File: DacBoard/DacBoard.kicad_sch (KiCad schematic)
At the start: 13 parts, among them J1 DacConnector, U1 74HC00, U2 AD688, U3 74HC00

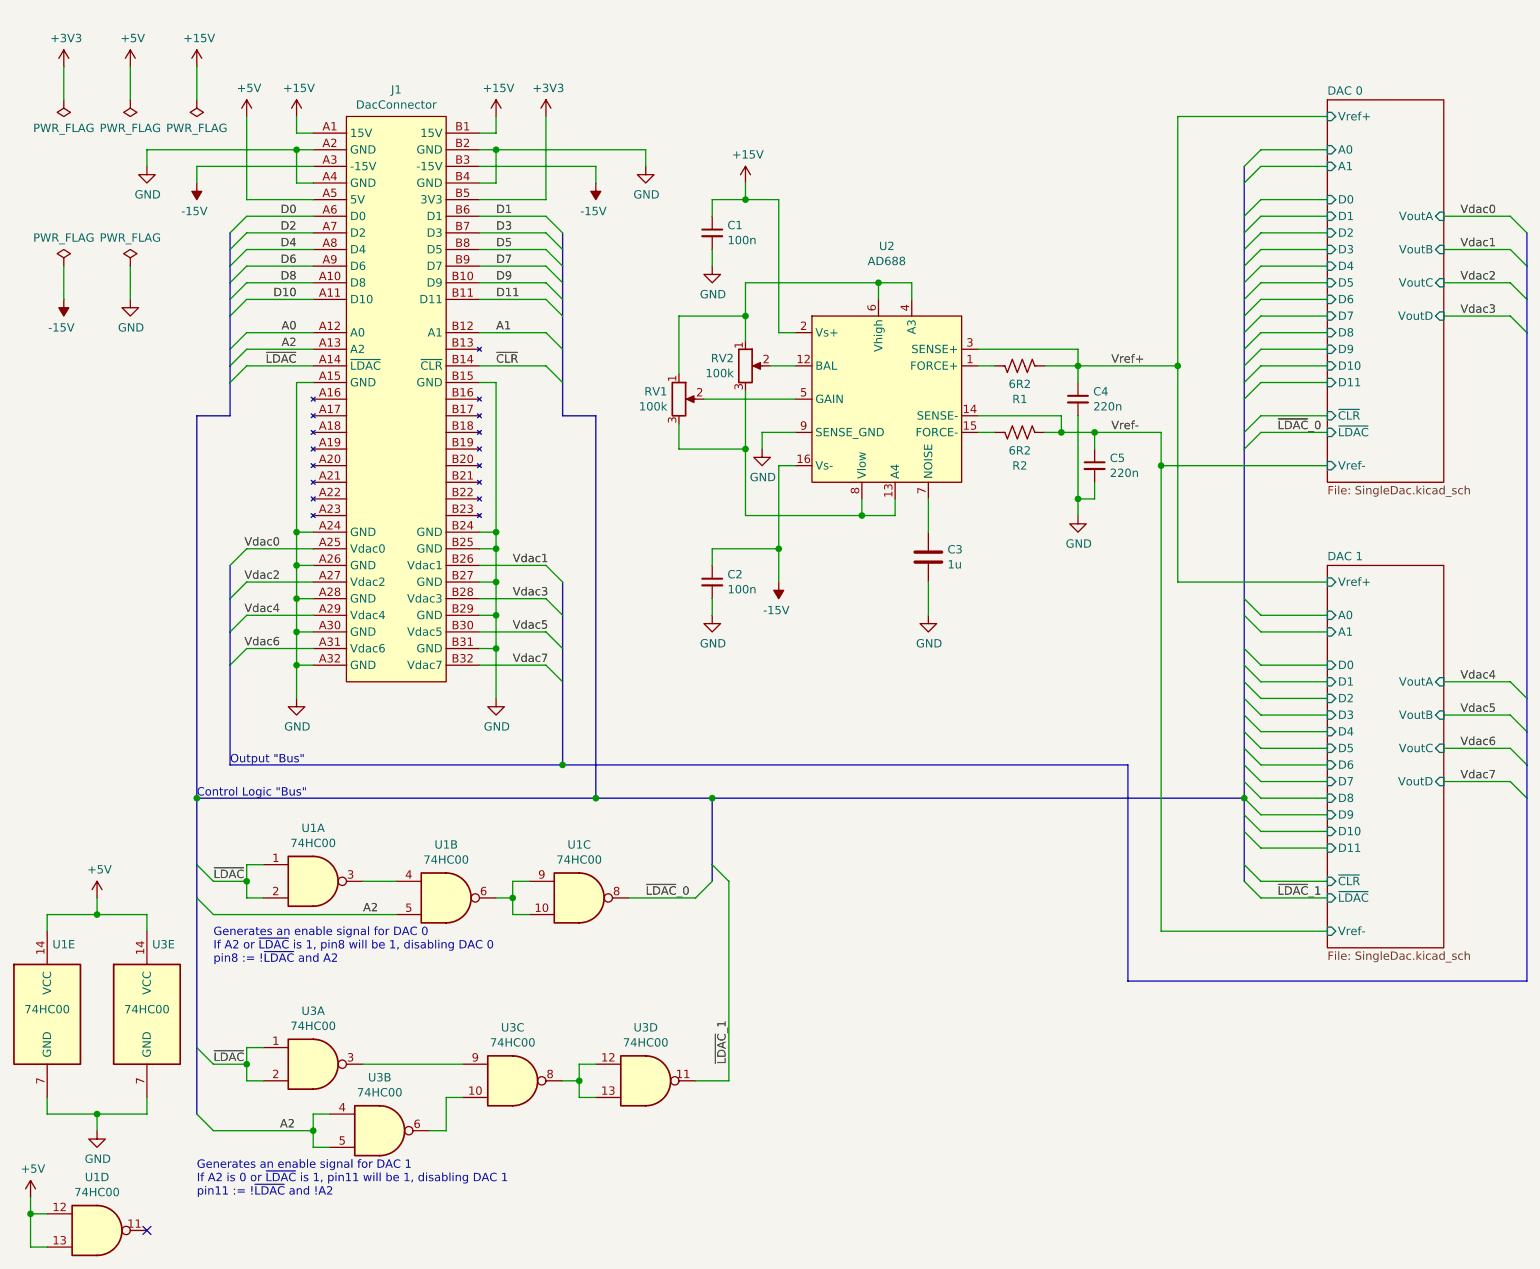
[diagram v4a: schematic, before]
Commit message: Added bypass caps and moved PWR_FLAGs around
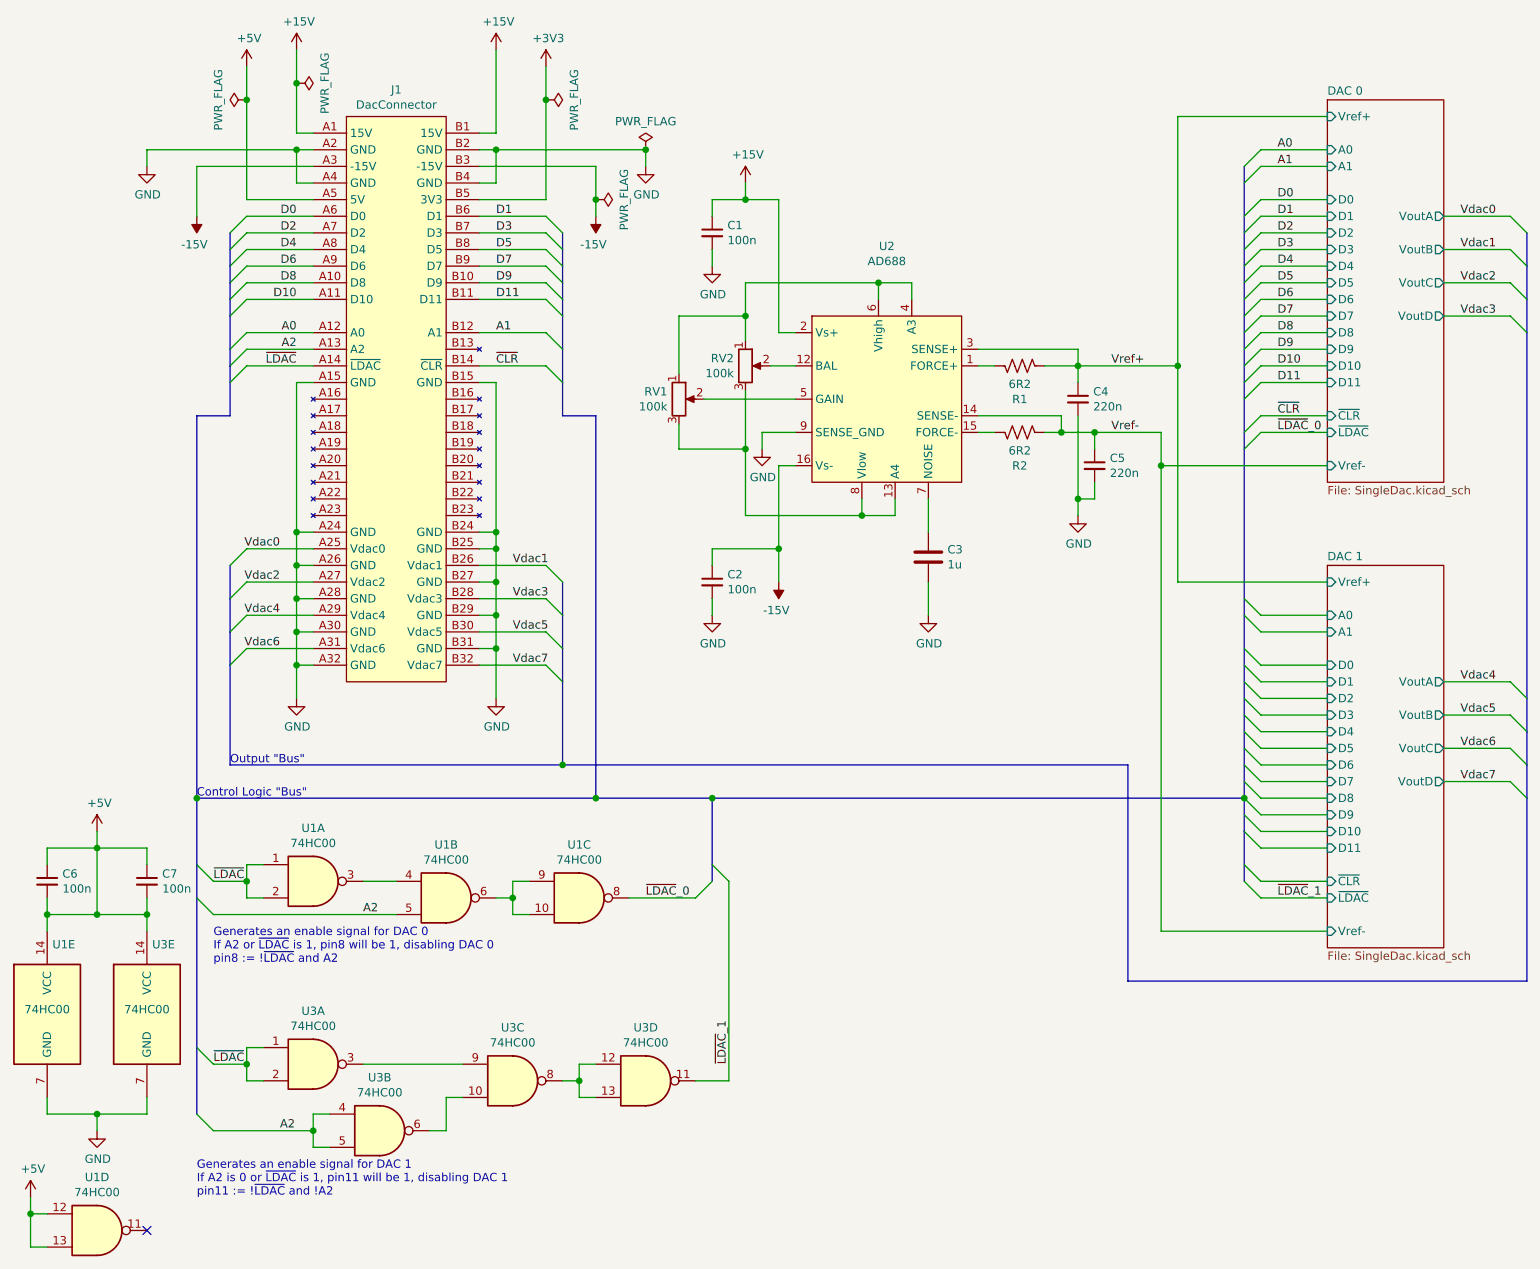
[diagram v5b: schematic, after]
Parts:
- added C6, C7: 100n, symbol Device:C_Small
- C1, C2, C3, C4, C5: footprint (none) -> Capacitor_SMD:C_0805_2012Metric_Pad1.18x1.45mm_HandSolder
- R1, R2: footprint (none) -> Resistor_SMD:R_0805_2012Metric_Pad1.20x1.40mm_HandSolder
- RV1, RV2: footprint (none) -> Potentiometer_SMD:Potentiometer_Bourns_TC33X_Vertical
- U1, U3: footprint (none) -> Package_SO:SOIC-14_3.9x8.7mm_P1.27mm
- U2: footprint (none) -> Package_SO:SOIC-16W_7.5x10.3mm_P1.27mm
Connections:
- net +5V: now also C6.1, C6.2, C7.1, C7.2

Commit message: Fixed description of enable signal generators
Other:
- note added: "Generates an enable signal for DAC 0 If A2 or ~LDAC is 1, pin8 will be 1, disabling DAC 0 pin8 := !(!~LDAC and A2)"
- note added: "Generates an enable signal for DAC 1 If A2 is 0 or ~LDAC is 1, pin11 will be 1, disabling DAC 1 pin11 := !(!~LDAC and !A2)"
- note removed: "Generates an enable signal for DAC 0 If A2 or ~LDAC is 1, pin8 will be 1, disabling DAC 0 pin8 := !~LDAC and A2"
- note removed: "Generates an enable signal for DAC 1 If A2 is 0 or ~LDAC is 1, pin11 will be 1, disabling DAC 1 pin11 := !~LDAC and !A2"
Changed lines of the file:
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@@
     (effects (font (size 1.27 1.27)) (justify left bottom))
   )
-  (text "Generates an enable signal for DAC 1\nIf A2 is 0 or ~LDAC is 1, pin11 will be 1, disabling DAC 1\npin11 := !~LDAC and !A2"
+  (text "Generates an enable signal for DAC 1\nIf A2 is 0 or ~LDAC is 1, pin11 will be 1, disabling DAC 1\npin11 := !(!~LDAC and !A2)"
     (at 40.64 193.04 0)
     (effects (font (size 1.27 1.27)) (justify left bottom))
   )
-  (text "Generates an enable signal for DAC 0\nIf A2 or ~LDAC is 1, pin8 will be 1, disabling DAC 0\npin8 := !~LDAC and A2"
+  (text "Generates an enable signal for DAC 0\nIf A2 or ~LDAC is 1, pin8 will be 1, disabling DAC 0\npin8 := !(!~LDAC and A2)"
     (at 43.18 157.48 0)
     (effects (font (size 1.27 1.27)) (justify left bottom))

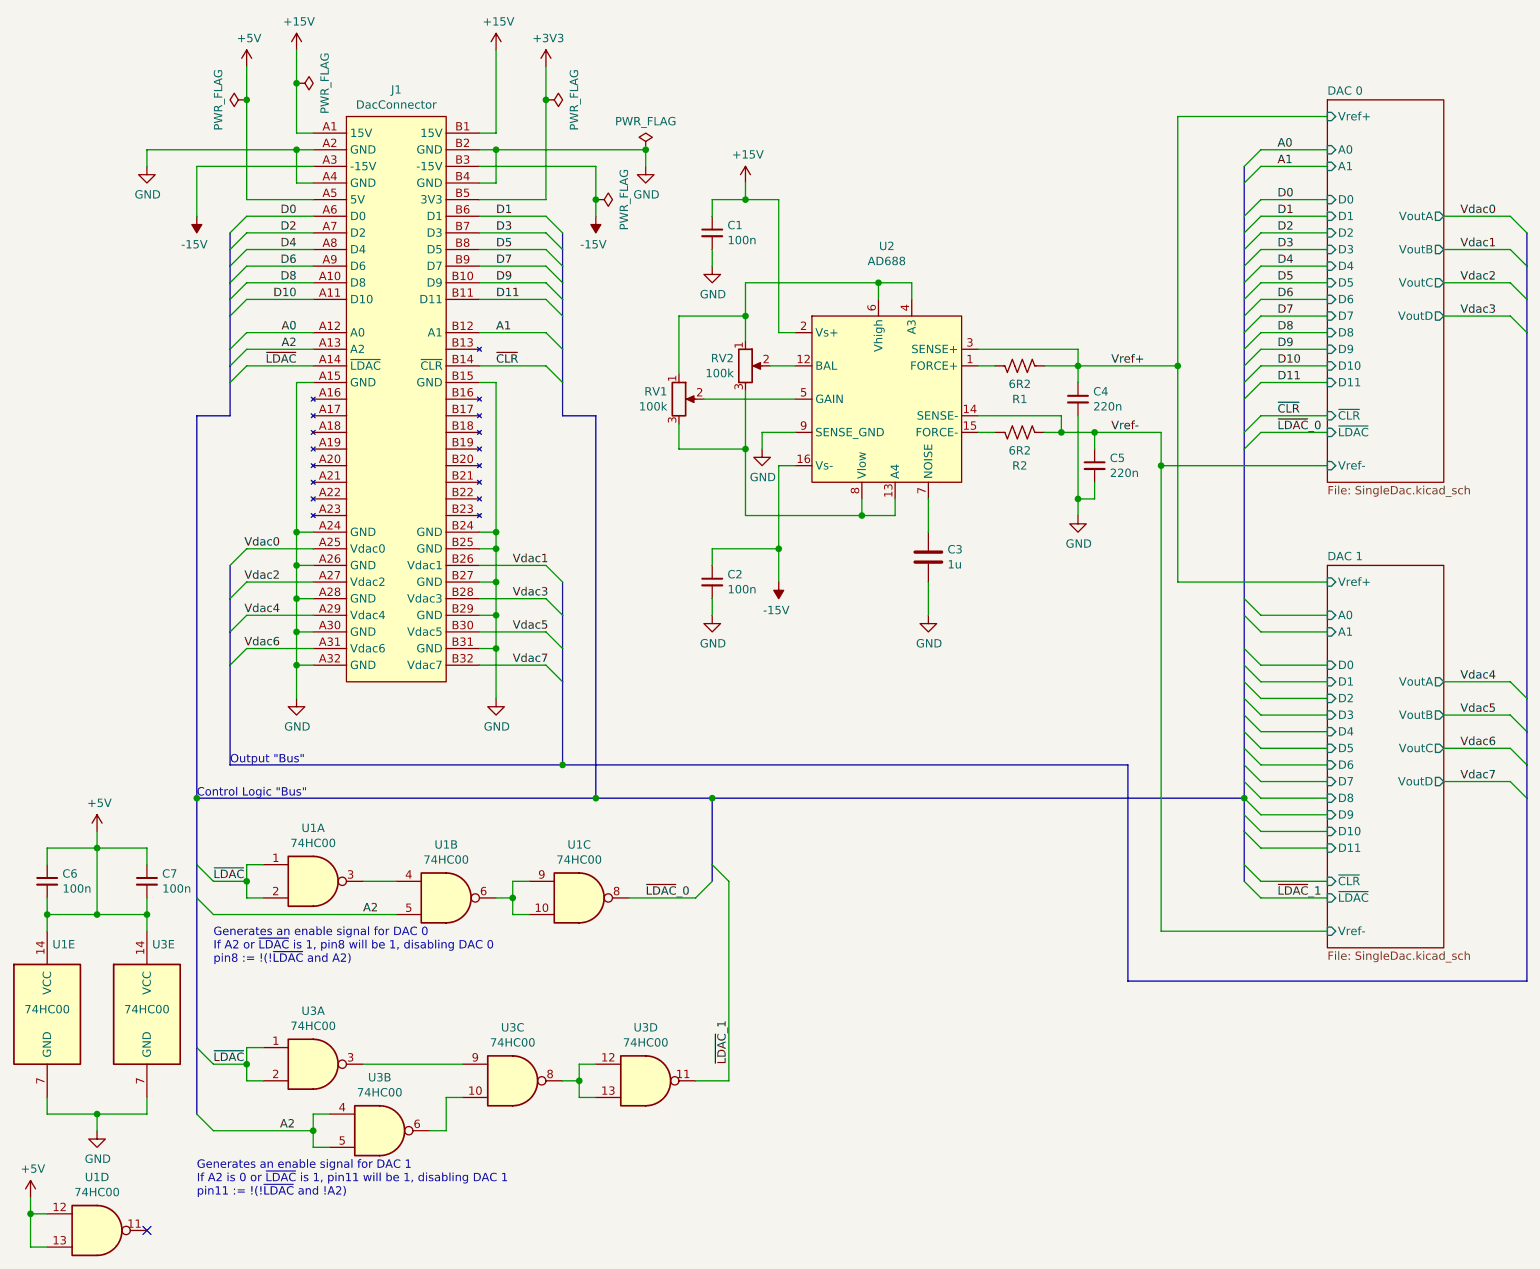
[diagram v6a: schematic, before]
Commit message: Schematic finalized (for now); Begin PCB
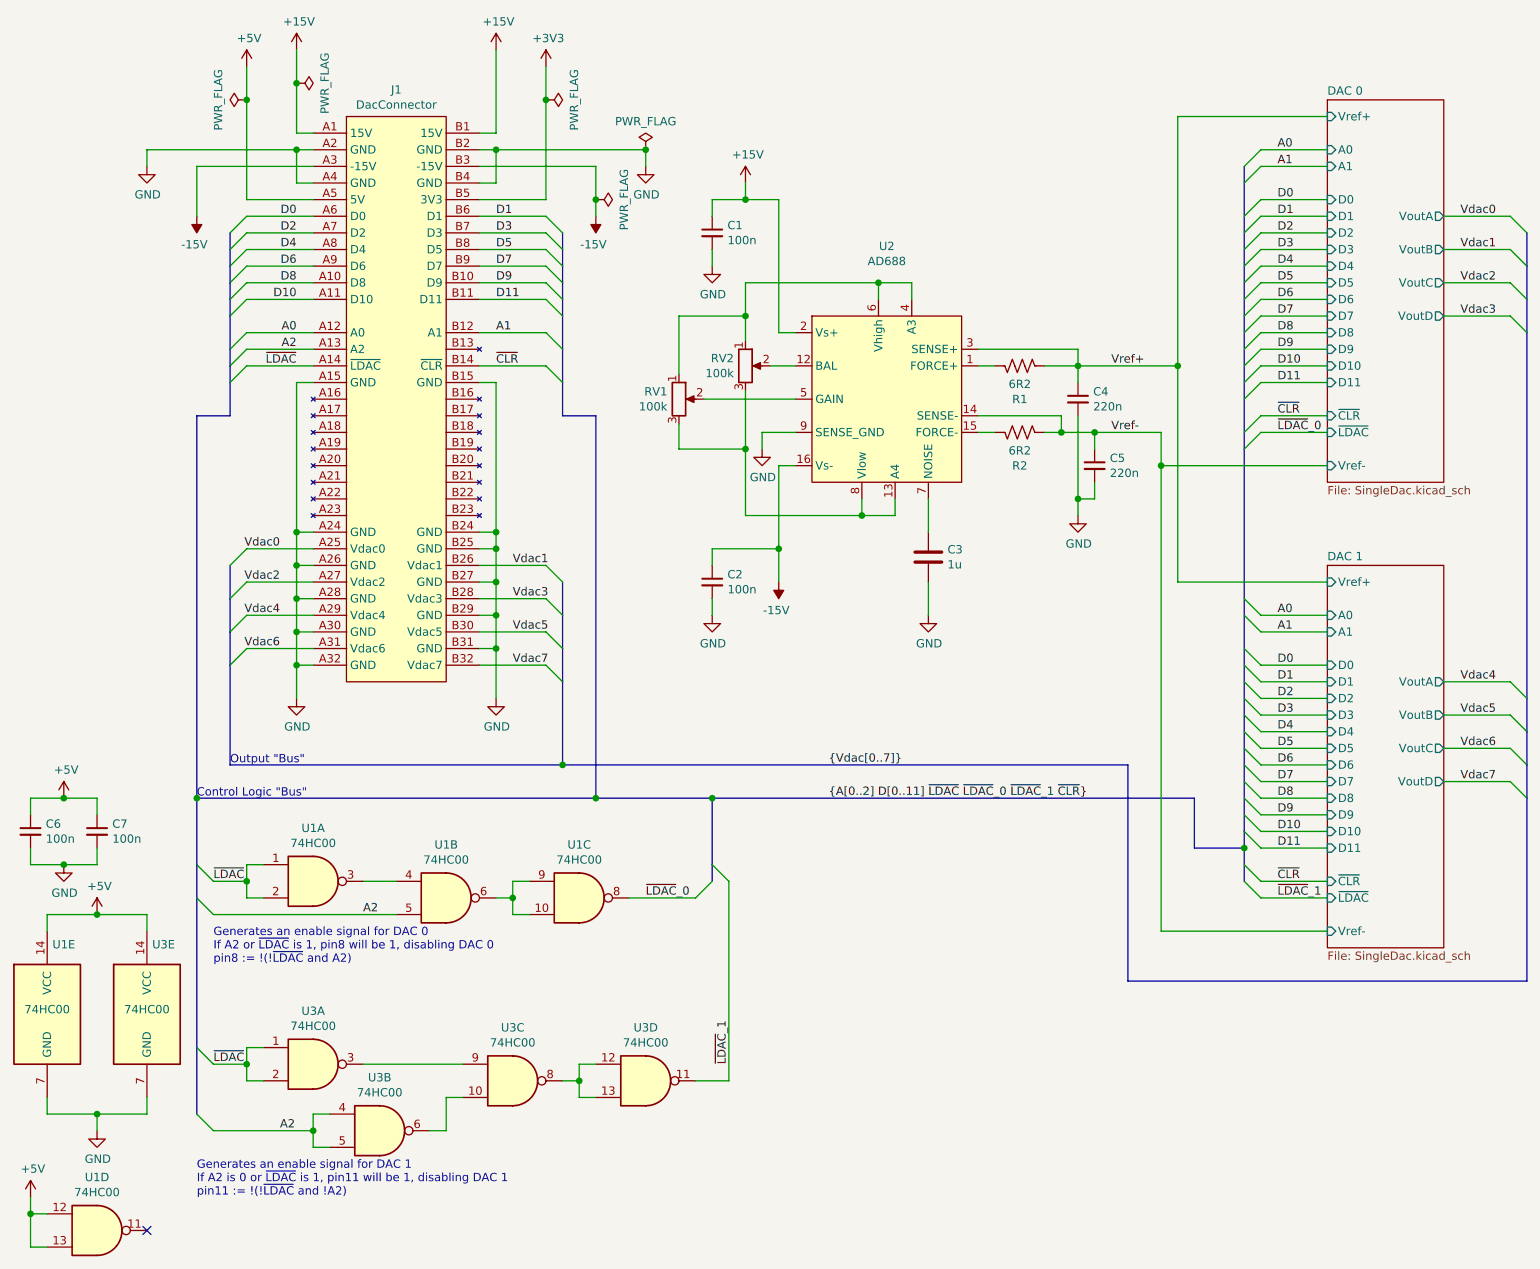
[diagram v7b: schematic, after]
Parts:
- C6, C7: footprint (none) -> Capacitor_SMD:C_0805_2012Metric_Pad1.18x1.45mm_HandSolder
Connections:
- net +5V: no longer C6.2, C7.2
- net GND: now also C6.2, C7.2
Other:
- moved on the sheet: C6, C7

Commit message: Working on PCB layout
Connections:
- net ~LDAC~_1: now also U3.8; no longer U3.11
- net at U3.9: now also U3.10, U3.11; no longer U3.3
- net at U3.6: now also U3.12; no longer U3.10
- new net: U3.13, U3.3
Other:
- note added: "Generates an enable signal for DAC 1 If A2 is 0 or ~LDAC is 1, pin11 will be 1, disabling DAC 1 pin8 := !(!~LDAC and !A2)"
- note removed: "Generates an enable signal for DAC 1 If A2 is 0 or ~LDAC is 1, pin11 will be 1, disabling DAC 1 pin11 := !(!~LDAC and !A2)"
- moved on the sheet: U3C, U3D
